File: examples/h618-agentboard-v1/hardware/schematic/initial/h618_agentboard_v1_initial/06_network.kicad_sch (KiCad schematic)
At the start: 1 part, among them U5 Gigabit PHY

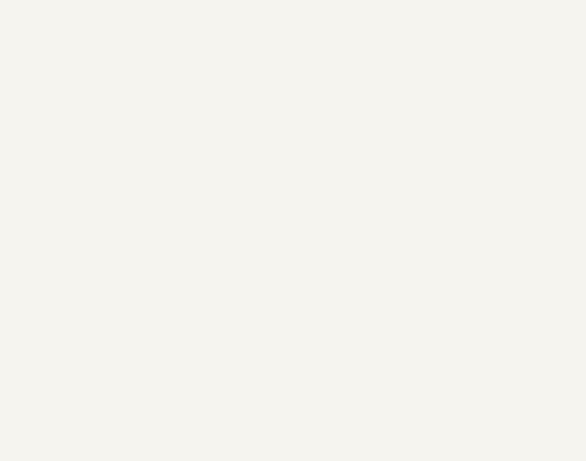
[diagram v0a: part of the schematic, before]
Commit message: feat(h618): consolidate schematic sheets / 整理原理图分页
将 H618 KiCad 原理图从大量小分图整理为 8 个可评审模块页，补充分图 profile 和回归测试，并同步 H618 文档、模型、example 工程与 where 进度。

Consolidate the H618 KiCad schematic into eight reviewable module sheets, add sheet grouping coverage, and sync the H618 model, docs, generated example project, and where progress.
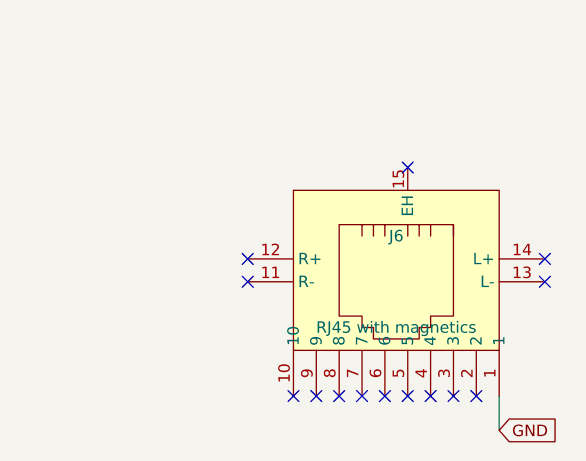
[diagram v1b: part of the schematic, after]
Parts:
- added J6: RJ45 with magnetics, JLC-MCP:RJ45-SMD_HC-RJ45-511Q-1-2, symbol jlc_symbols:HC-RJ45-511Q-1-2
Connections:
- net GND: now also J6.1
- no-connect marks 22 -> 36
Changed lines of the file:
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@@
     (instances
       (project "h618_agentboard_v1_initial"
-        (path "/37187014-47b7-426d-9def-02aac6df84ab"
+        (path "/fcb348bb-564f-4098-b5c7-3bfd0080ba4f"
           (reference "U5")
           (unit 1)
@@
     )
   )
+  (symbol
+    (lib_id "jlc_symbols:HC-RJ45-511Q-1-2")
+    (at 180.34 355.6 0)
+    (unit 1)
+    (exclude_from_sim no)
+    (in_bom yes)
+    (on_board yes)
+    (dnp no)
+    (property "Reference" "J6" (at 180.34 350.52 0)
+      (effects (font (size 1.27 1.27)))
+    )
+    (property "Value" "RJ45 with magnetics" (at 180.34 360.68 0)
+      (effects (font (size 1.27 1.27)))
+    )
+    (property "Footprint" "JLC-MCP:RJ45-SMD_HC-RJ45-511Q-1-2" (at 180.34 355.6 0)
+      (hide yes)
+      (effects (font (size 1.27 1.27)))
+    )
+      (property "LCSC" "C42376615" (at 0 0 0)
+        (hide yes)
+        (effects (font (size 1.27 1.27)))
+      )
+      (pin "1")
+      (pin "2")
+      (pin "3")
+      (pin "4")
+      (pin "5")
+      (pin "6")
+      (pin "7")
+      (pin "8")
+      (pin "9")
+      (pin "10")
+      (pin "11")
+      (pin "12")
+      (pin "13")
+      (pin "14")
+      (pin "15")
+    (instances
+      (project "h618_agentboard_v1_initial"
+        (path "/fcb348bb-564f-4098-b5c7-3bfd0080ba4f"
+          (reference "J6")
+          (unit 1)
+        )
+      )
+    )
+  )
   (wire (pts (xy 26.67 53.34) (xy 22.86 53.34))
     (stroke (width 0) (type default))
@@
   )
   (no_connect (at 74.93 30.48)
+  )
+  (wire (pts (xy 191.77 368.3) (xy 191.77 372.11))
+    (stroke (width 0) (type default))
+  )
+  (global_label "GND" (shape input) (at 191.77 372.11 0)
+    (effects (font (size 1.27 1.27)))
+  )
+  (no_connect (at 189.23 368.3)
+  )
+  (no_connect (at 186.69 368.3)
+  )
+  (no_connect (at 184.15 368.3)
+  )
+  (no_connect (at 181.61 368.3)
+  )
+  (no_connect (at 179.07 368.3)
+  )
+  (no_connect (at 176.53 368.3)
+  )
+  (no_connect (at 173.99 368.3)
+  )
+  (no_connect (at 171.45 368.3)
+  )
+  (no_connect (at 168.91 368.3)
+  )
+  (no_connect (at 163.83 355.6)
+  )
+  (no_connect (at 163.83 353.06)
+  )
+  (no_connect (at 196.85 355.6)
+  )
+  (no_connect (at 196.85 353.06)
+  )
+  (no_connect (at 181.61 342.9)
   )
   (sheet_instances
     (path "/" (page "1"))
-    (path "/94ec4ba8-0126-4b72-8105-27894cd12c75" (page "2"))
-    (path "/e98a2a13-8b29-457f-955f-03d2c9361488" (page "3"))
-    (path "/730b730e-bfa6-4d2d-bbb0-e112bcf09da6" (page "4"))
-    (path "/31b33f30-46c8-4fe1-be2c-d06fbbbc0992" (page "5"))
-    (path "/d4cd7712-a2fd-4ddd-bb20-7febf5987c70" (page "6"))
-    (path "/699a46a6-ff10-4909-8728-1ab9ffb9d84f" (page "7"))
-    (path "/f196dda9-3b90-488a-b9c2-c20a603e71cd" (page "8"))
-    (path "/7cb1a180-4587-43a5-a744-9f84b2df6ecb" (page "9"))
-    (path "/51fc19cf-0146-4c44-a72e-feda708a6ee9" (page "10"))
-    (path "/284603d0-b29d-4586-ab56-8c2a8e119254" (page "11"))
-    (path "/0ab9fde6-bb51-4815-aa9c-27ac4cc39537" (page "12"))
-    (path "/211866ae-7629-420e-a86d-ecc98ddd5dcd" (page "13"))
-    (path "/54a43287-d964-4df7-9e7e-d1b6e1a5c407" (page "14"))
-    (path "/16bf6aeb-1d74-4e72-9de7-3b5c5b462401" (page "15"))
-    (path "/c85b3663-d33a-4960-af7d-36d6ae3cd2c2" (page "16"))
-    (path "/e6e1dded-653d-4511-b0b9-d99eb53590cb" (page "17"))
-    (path "/a91a95df-0a8b-46e3-85af-d117d6527513" (page "18"))
-    (path "/d666a00d-e870-4011-bf97-806ccc844320" (page "19"))
-    (path "/36a80770-0baf-4ee9-bfc1-89e10be33f0f" (page "20"))
-    (path "/dcd1f680-1af9-4b96-b000-b126327c377d" (page "21"))
-    (path "/990cd876-4da3-44cb-9d49-465c9c58dbd1" (page "22"))
-    (path "/a1a65ab4-5c22-49ba-a94a-582862ddaabc" (page "23"))
-    (path "/33a26f35-1c34-4e7a-a246-c7f2b2aedc8a" (page "24"))
-    (path "/7c35330c-efa0-42f9-af03-91dbbec74bc4" (page "25"))
-    (path "/37187014-47b7-426d-9def-02aac6df84ab" (page "26"))
-    (path "/0e905d2b-cc9f-483e-bc91-a4ee5dc5583e" (page "27"))
-    (path "/94474b9d-06b4-4eba-afd8-90248a871b4f" (page "28"))
-    (path "/4d4e7766-7db8-4a24-9bb5-123c2358fc4d" (page "29"))
-    (path "/4a3e4fe3-0361-497b-8723-f2ae2e776ac0" (page "30"))
-    (path "/692f04a6-2b7b-4ef6-8bbf-28caa424d308" (page "31"))
-    (path "/1ffd4b7b-2d9b-4897-be72-02fffbf8d6ef" (page "32"))
-    (path "/3818267b-9044-43b2-ad1b-fd47d020acd3" (page "33"))
-    (path "/576d9598-8523-49fa-a42c-069069795c6a" (page "34"))
+    (path "/d6058d2c-1e39-450a-a98b-f7e0b567bb2e" (page "2"))
+    (path "/94b8340a-a88c-4351-9eb7-1caf1e9eb372" (page "3"))
+    (path "/86a79d61-8b0d-4adc-9d5d-e43a8a670b13" (page "4"))
+    (path "/50c7ea96-48ca-4f0d-89a0-adb76130baec" (page "5"))
+    (path "/46d738dc-892e-4135-8263-520e3eb36067" (page "6"))
+    (path "/fcb348bb-564f-4098-b5c7-3bfd0080ba4f" (page "7"))
+    (path "/6d2f9a3c-19cb-45b7-8c63-c77e10ed64a0" (page "8"))
+    (path "/c0c26f21-8c44-4dce-8530-33cef538296f" (page "9"))
   )
 )
